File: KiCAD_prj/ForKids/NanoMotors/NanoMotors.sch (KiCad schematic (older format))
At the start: 25 parts

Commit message: Update Nano Motors project
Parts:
- added J10, J9: Conn_01x15_Female, symbol Connector:Conn_01x15_Female
- gave numbers to parts that had none: 25
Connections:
- net labels added: 3V3, A0, A1, A2, A3, A4, A5, A6, A7, AREF, VIN
- wire segments 158 -> 205
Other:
- moved on the sheet: A1, C1, C2, C3, D1, D2, J1, J2, J3, J4, J5, J6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

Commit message: Update NanoMotors project
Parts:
- removed J10, J2: Conn_01x15_Female, symbol Connector:Conn_01x15_Female
- removed SW1: SW_SPDT, Connector_PinHeader_1.00mm:PinHeader_1x03_P1.00mm_Vertical, symbol Switch:SW_SPDT
- added J4, J5: Conn_01x15_Female, Connector_PinHeader_2.54mm:PinHeader_1x15_P2.54mm_Vertical, symbol Connector:Conn_01x15_Female
- added SW1: SW_DPST_x2, Connector_PinHeader_2.54mm:PinHeader_1x03_P2.54mm_Vertical, symbol Switch:SW_DPST_x2
- C1: footprint (none) -> Capacitor_THT:CP_Radial_D6.3mm_P2.50mm
- C2: renamed from C3; footprint (none) -> Capacitor_THT:CP_Radial_D6.3mm_P2.50mm
- C3: renamed from C2; footprint (none) -> Capacitor_THT:CP_Radial_D6.3mm_P2.50mm
- J1: renamed from J4; footprint (none) -> Connector_PinHeader_2.54mm:PinHeader_1x15_P2.54mm_Vertical
- J10: renamed from J8; value Screw_Terminal_01x02 -> M1
- J2: renamed from J1; footprint (none) -> Connector_PinHeader_2.54mm:PinHeader_1x15_P2.54mm_Vertical
- J3: footprint (none) -> Connector_PinHeader_2.54mm:PinHeader_1x15_P2.54mm_Vertical
- J6: renamed from J9; footprint (none) -> Connector_PinHeader_2.54mm:PinHeader_1x15_P2.54mm_Vertical
- J9: renamed from J7; value Screw_Terminal_01x02 -> M2
- Q1, Q2: footprint Package_TO_SOT_THT:TO-92_Inline -> Package_TO_SOT_THT:TO-92_Inline_Wide
- R1, R2, R3, R4, R5, R6: footprint (none) -> Resistor_THT:R_Axial_DIN0309_L9.0mm_D3.2mm_P12.70mm_Horizontal
- renumbered J5 to J7, J6 to J8
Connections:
- net labels removed: 11, 12
- wire segments 205 -> 211
- no-connect marks 1 -> 2
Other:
- note added: "M1"
- note added: "M2"
- note added: "Внешнее электропитание платы"
- note added: "Драйвер мотора"
- note added: "Реверс моторов"
- note added: "Шины питания"
- moved on the sheet: A1, C1, C2, C3, D1, D2, J1, J10, J2, J3, J6, J7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

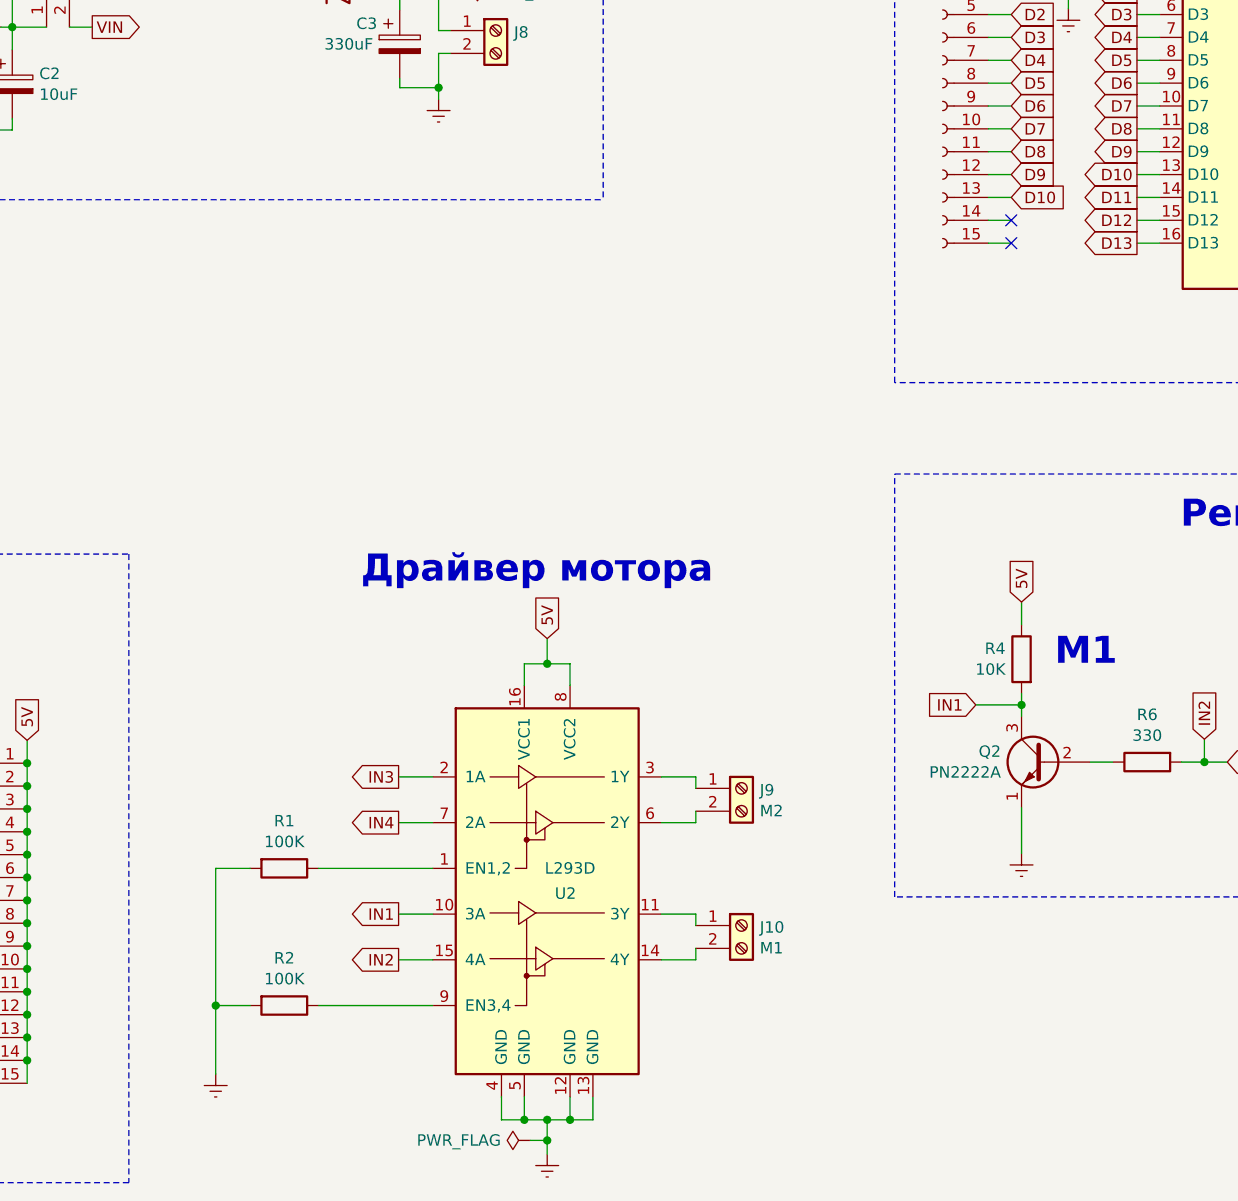
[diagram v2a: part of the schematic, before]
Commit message: Update NanoMotors project: fix D10 D9 pins
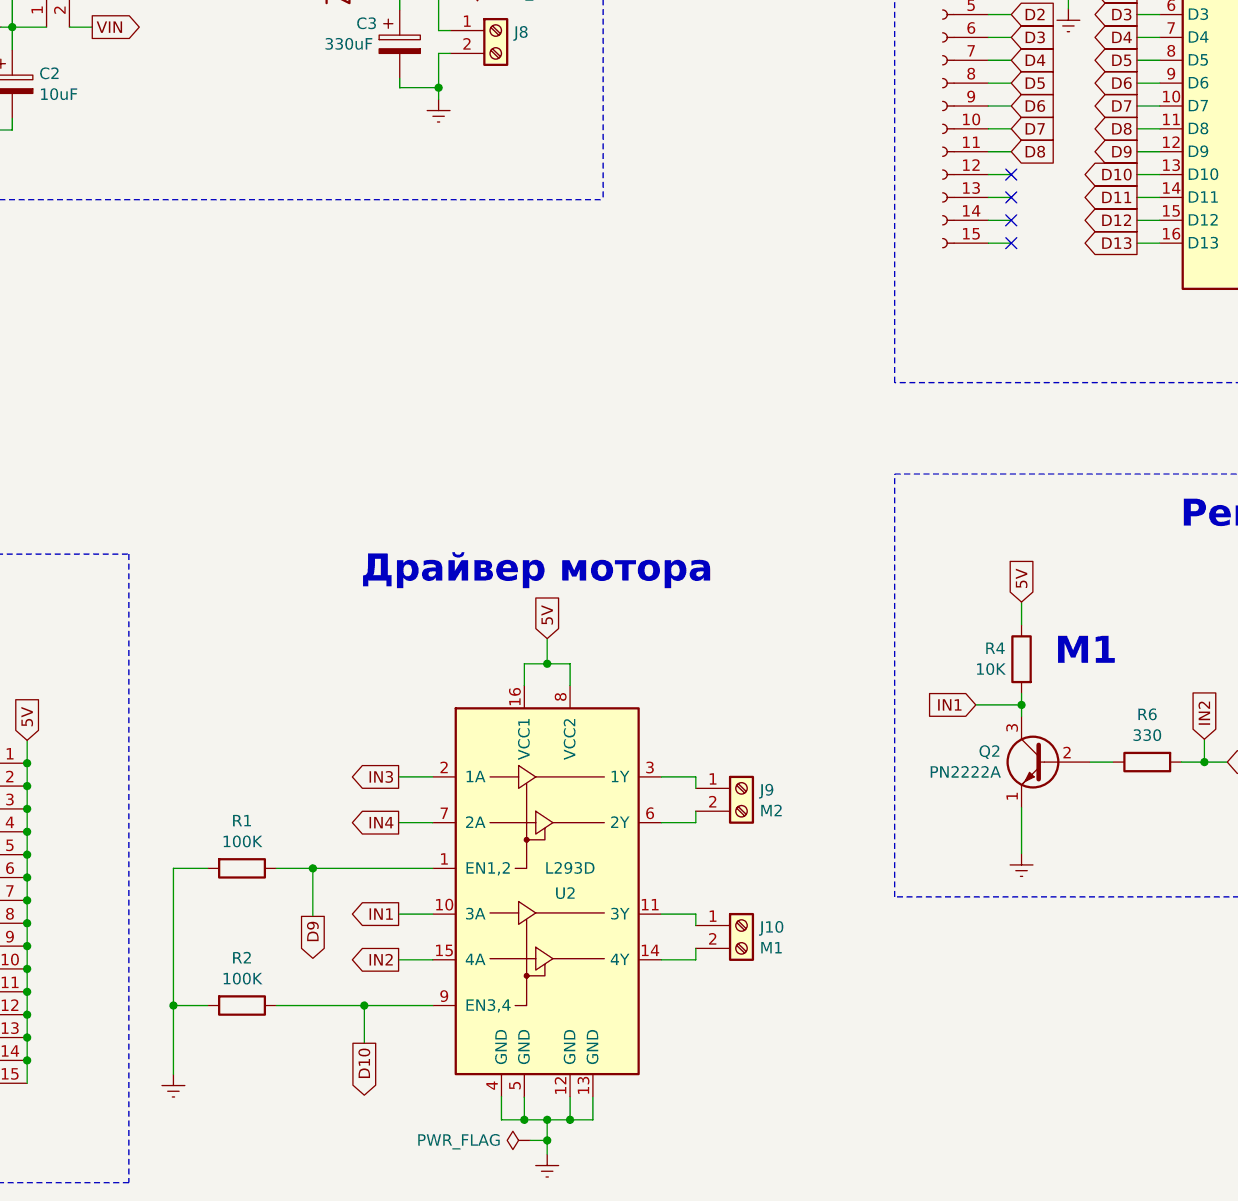
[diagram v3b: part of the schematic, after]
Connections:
- net D10: now also R2.1, U2.9 (EN3,4); no longer J1.13 (Pin_13)
- net D9: now also R1.1, U2.1 (EN1,2); no longer J1.12 (Pin_12)
- no-connect marks 2 -> 4
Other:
- moved on the sheet: R1, R2
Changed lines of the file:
@@
 L Device:R R1
 U 1 1 5F7CA298
-P 4130 6075
-F 0 "R1" V 3923 6075 50  0000 C CNN
-F 1 "100K" V 4014 6075 50  0000 C CNN
-F 2 "Resistor_THT:R_Axial_DIN0309_L9.0mm_D3.2mm_P12.70mm_Horizontal" V 4060 6075 50  0001 C CNN
-F 3 "~" H 4130 6075 50  0001 C CNN
-	1    4130 6075
+P 3945 6075
+F 0 "R1" V 3738 6075 50  0000 C CNN
+F 1 "100K" V 3829 6075 50  0000 C CNN
+F 2 "Resistor_THT:R_Axial_DIN0309_L9.0mm_D3.2mm_P12.70mm_Horizontal" V 3875 6075 50  0001 C CNN
+F 3 "~" H 3945 6075 50  0001 C CNN
+	1    3945 6075
 	0    1    1    0
 $EndComp
@@
 L Device:R R2
 U 1 1 5F7CB336
-P 4130 6675
-F 0 "R2" V 3923 6675 50  0000 C CNN
-F 1 "100K" V 4014 6675 50  0000 C CNN
-F 2 "Resistor_THT:R_Axial_DIN0309_L9.0mm_D3.2mm_P12.70mm_Horizontal" V 4060 6675 50  0001 C CNN
-F 3 "~" H 4130 6675 50  0001 C CNN
-	1    4130 6675
+P 3945 6675
+F 0 "R2" V 3738 6675 50  0000 C CNN
+F 1 "100K" V 3829 6675 50  0000 C CNN
+F 2 "Resistor_THT:R_Axial_DIN0309_L9.0mm_D3.2mm_P12.70mm_Horizontal" V 3875 6675 50  0001 C CNN
+F 3 "~" H 3945 6675 50  0001 C CNN
+	1    3945 6675
 	0    1    1    0
 $EndComp
@@
 L power:Earth #PWR010
 U 1 1 5F7CCC0C
-P 3830 6975
-F 0 "#PWR010" H 3830 6725 50  0001 C CNN
-F 1 "Earth" H 3830 6825 50  0001 C CNN
-F 2 "" H 3830 6975 50  0001 C CNN
-F 3 "~" H 3830 6975 50  0001 C CNN
-	1    3830 6975
-	1    0    0    -1
-$EndComp
-Wire Wire Line
-	3830 6975 3830 6675
-Wire Wire Line
-	3830 6075 3980 6075
-Wire Wire Line
-	3980 6675 3830 6675
-Connection ~ 3830 6675
-Wire Wire Line
-	3830 6675 3830 6075
+P 3645 6975
+F 0 "#PWR010" H 3645 6725 50  0001 C CNN
+F 1 "Earth" H 3645 6825 50  0001 C CNN
+F 2 "" H 3645 6975 50  0001 C CNN
+F 3 "~" H 3645 6975 50  0001 C CNN
+	1    3645 6975
+	1    0    0    -1
+$EndComp
+Wire Wire Line
+	3645 6975 3645 6675
+Wire Wire Line
+	3645 6075 3795 6075
+Wire Wire Line
+	3795 6675 3645 6675
+Connection ~ 3645 6675
+Wire Wire Line
+	3645 6675 3645 6075
 $Comp
 L Connector:Screw_Terminal_01x02 J10
@@
 Wire Wire Line
 	4630 5675 4780 5675
-Wire Wire Line
-	4280 6075 4780 6075
-Wire Wire Line
-	4280 6675 4780 6675
 Wire Wire Line
 	4630 5875 4780 5875
@@
 Wire Wire Line
 	7310 2740 7210 2740
-Text GLabel 7310 3040 2    50   Input ~ 0
-D9
 Wire Wire Line
 	7310 2840 7210 2840
-Text GLabel 7310 3140 2    50   Input ~ 0
-D10
 Wire Wire Line
 	7310 2940 7210 2940
@@
 Text Notes 4465 4840 0    118  ~ 24
 Драйвер мотора
+Text GLabel 4480 6840 3    50   Output ~ 0
+D10
+Wire Wire Line
+	4480 6840 4480 6675
+Wire Wire Line
+	4480 6675 4780 6675
+Wire Wire Line
+	4095 6075 4255 6075
+Wire Wire Line
+	4095 6675 4480 6675
+Connection ~ 4480 6675
+Text GLabel 4255 6285 3    50   Output ~ 0
+D9
+Wire Wire Line
+	4255 6285 4255 6075
+Connection ~ 4255 6075
+Wire Wire Line
+	4255 6075 4780 6075
+NoConn ~ 7310 3140
+NoConn ~ 7310 3040
 $EndSCHEMATC
